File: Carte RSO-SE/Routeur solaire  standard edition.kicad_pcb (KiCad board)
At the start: 2 copper layers, 127.6 x 203.2 mm, 57 parts

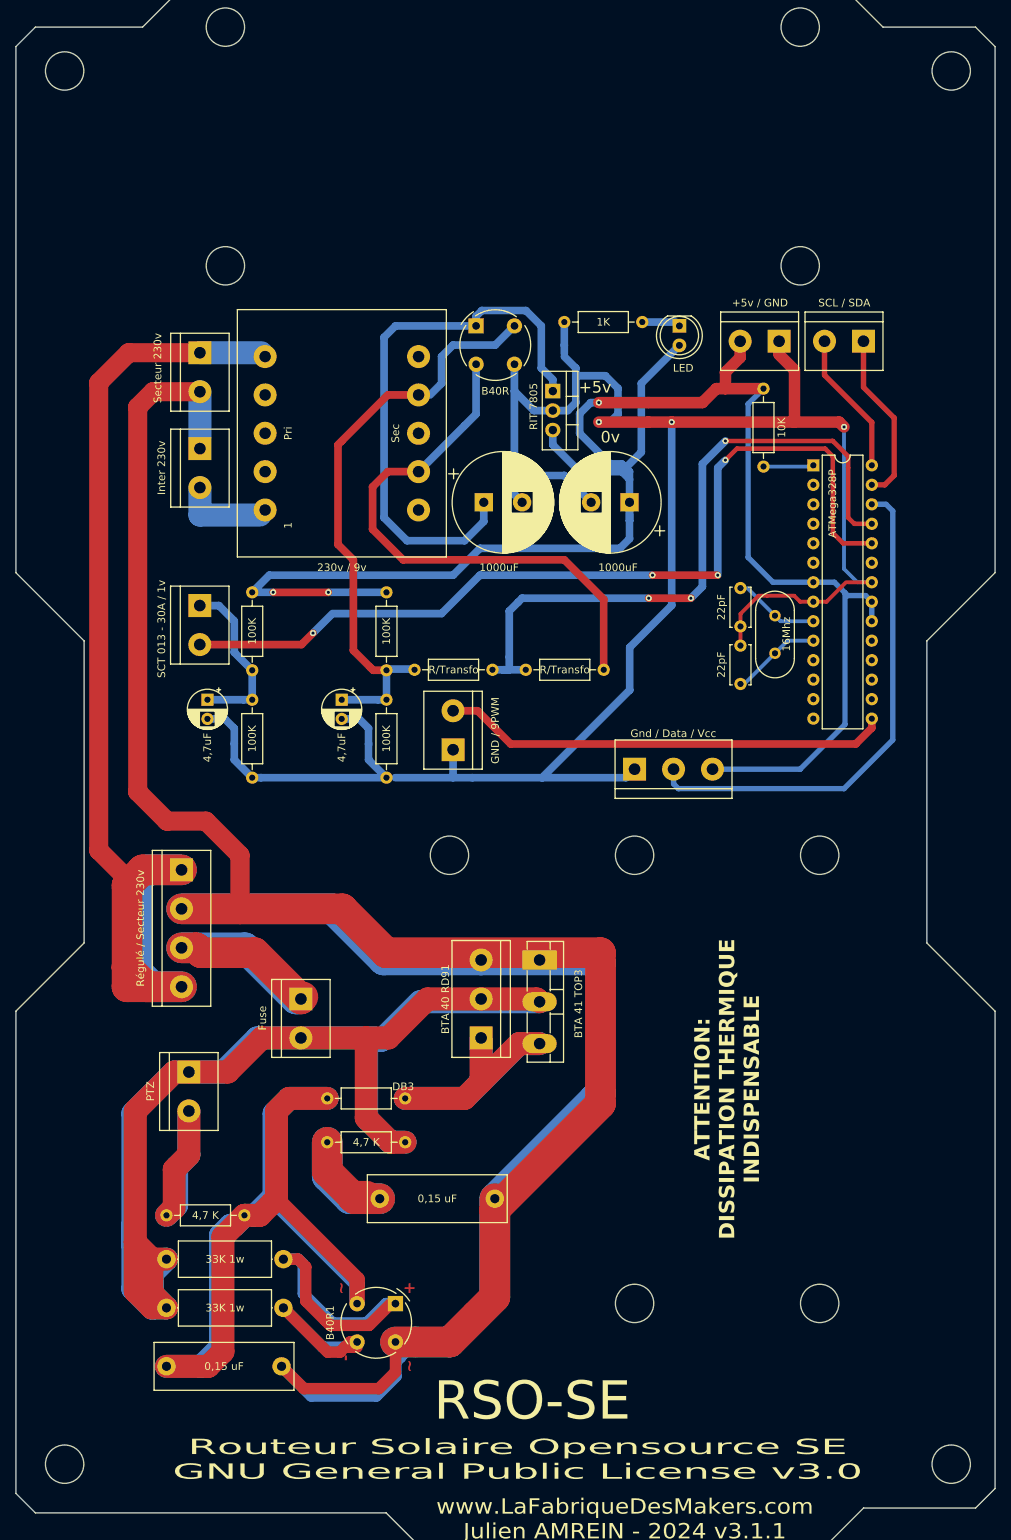
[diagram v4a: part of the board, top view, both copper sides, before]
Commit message: Bornier détection heures creuses
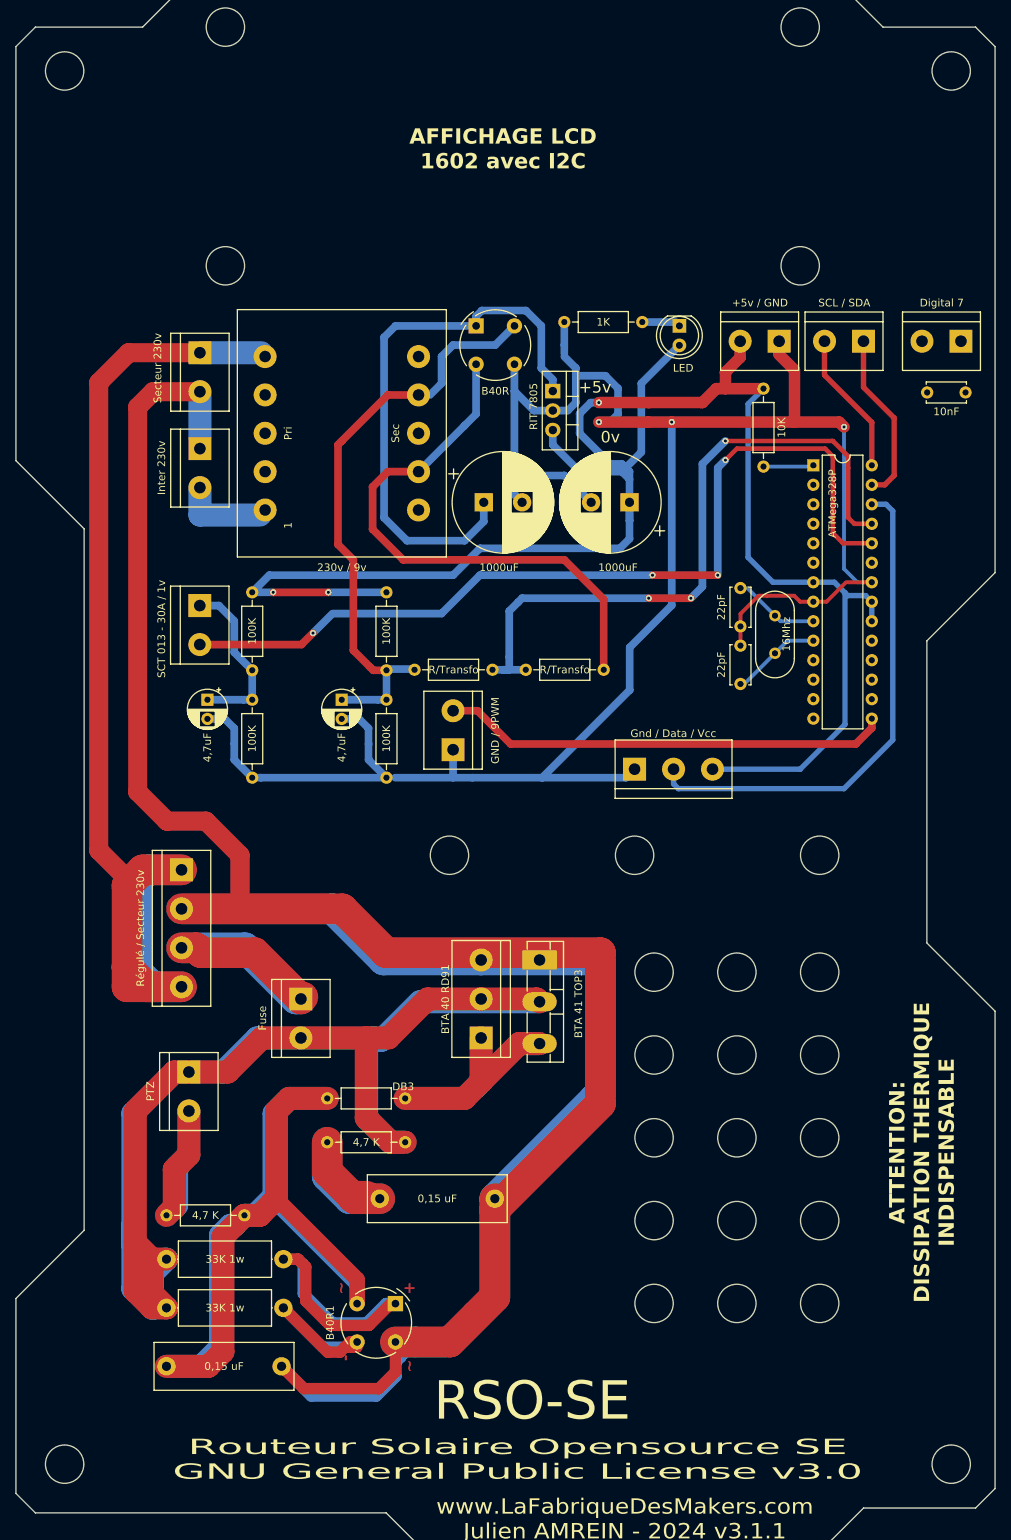
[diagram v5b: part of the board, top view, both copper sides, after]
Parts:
- removed the ? at (-53.3, 167.6)
- added 10nF: C_Disc_D5.0mm_W2.5mm_P5.00mm, Capacitor_THT:C_Disc_D5.0mm_W2.5mm_P5.00mm, F.Cu at (-15.2, 48.9)
- added ?: MountingHole_5mm, MountingHole:MountingHole_5mm, F.Cu at (-50.8, 156.8)
- added ?: MountingHole_5mm, MountingHole:MountingHole_5mm, F.Cu at (-40.0, 124.5)
- added ?: MountingHole_5mm, MountingHole:MountingHole_5mm, F.Cu at (-29.2, 135.3)
- added ?: MountingHole_5mm, MountingHole:MountingHole_5mm, F.Cu at (-29.2, 124.5)
- added ?: MountingHole_5mm, MountingHole:MountingHole_5mm, F.Cu at (-29.2, 156.8)
- added ?: MountingHole_5mm, MountingHole:MountingHole_5mm, F.Cu at (-50.8, 124.5)
- added ?: MountingHole_5mm, MountingHole:MountingHole_5mm, F.Cu at (-40.0, 156.8)
- added ?: MountingHole_5mm, MountingHole:MountingHole_5mm, F.Cu at (-50.8, 135.3)
- added ?: MountingHole_5mm, MountingHole:MountingHole_5mm, F.Cu at (-40.0, 135.3)
- added ?: MountingHole_5mm, MountingHole:MountingHole_5mm, F.Cu at (-50.8, 146.1)
- added ?: MountingHole_5mm, MountingHole:MountingHole_5mm, F.Cu at (-40.0, 146.1)
- added ?: MountingHole_5mm, MountingHole:MountingHole_5mm, F.Cu at (-50.8, 167.6)
- added ?: MountingHole_5mm, MountingHole:MountingHole_5mm, F.Cu at (-40.0, 167.6)
- added ?: MountingHole_5mm, MountingHole:MountingHole_5mm, F.Cu at (-29.2, 146.1)
- added Digital 7: TerminalBlock_bornier-2_P5.08mm, TerminalBlock:TerminalBlock_bornier-2_P5.08mm, F.Cu at (-10.8, 42.2)
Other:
- outline, holes or cut-outs redrawn
- board text added: "AFFICHAGE LCD 1602 avec I2C"

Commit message: RSO Dark edition béta test
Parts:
- removed the 4,7 K at (-93.4, 146.6)
- removed the ? at (-50.8, 156.8)
- removed the ? at (-128.3, -83.8)
- removed the ? at (-29.2, 167.6)
- removed the ? at (-29.2, 124.5)
- removed the ? at (-29.2, 156.8)
- removed the ? at (-50.8, 124.5)
- removed the ? at (-53.3, -114.9)
- removed the ? at (-40.0, 156.8)
- removed the ? at (-53.3, -83.8)
- removed the ? at (-128.3, -114.9)
- removed the ? at (-50.8, 146.1)
- removed the ? at (-50.8, 167.6)
- removed the ? at (-40.0, 167.6)
- removed the ? at (-29.2, 146.1)
- added 10K: R_Axial_DIN0207_L6.3mm_D2.5mm_P10.16mm_Horizontal, Resistor_THT:R_Axial_DIN0207_L6.3mm_D2.5mm_P10.16mm_Horizontal, F.Cu at (-19.1, 48.3)
- added 4,7K: R_Axial_DIN0207_L6.3mm_D2.5mm_P10.16mm_Horizontal, Resistor_THT:R_Axial_DIN0207_L6.3mm_D2.5mm_P10.16mm_Horizontal, F.Cu at (-42.5, 90.8)
- added 4,7K 1w: R_Axial_DIN0414_L11.9mm_D4.5mm_P15.24mm_Horizontal, Resistor_THT:R_Axial_DIN0414_L11.9mm_D4.5mm_P15.24mm_Horizontal, F.Cu at (-93.3, 146.7)
- added ?: MountingHole_5mm, MountingHole:MountingHole_5mm, F.Cu at (-58.4, 5.71)
- added ?: MountingHole_5mm, MountingHole:MountingHole_5mm, F.Cu at (-90.8, 5.71)
- added ?: MountingHole_5mm, MountingHole:MountingHole_5mm, F.Cu at (-69.2, 24.8)
- added ?: MountingHole_5mm, MountingHole:MountingHole_5mm, F.Cu at (-69.2, 5.71)
- added ?: MountingHole_5mm, MountingHole:MountingHole_5mm, F.Cu at (-58.4, 24.8)
- added ?: MountingHole_5mm, MountingHole:MountingHole_5mm, F.Cu at (-47.6, 5.71)
- added ?: MountingHole_5mm, MountingHole:MountingHole_5mm, F.Cu at (-47.6, 24.8)
- added ?: MountingHole_5mm, MountingHole:MountingHole_5mm, F.Cu at (-80.0, 24.8)
- added ?: MountingHole_5mm, MountingHole:MountingHole_5mm, F.Cu at (-80.0, 5.71)
- added ?: MountingHole_5mm, MountingHole:MountingHole_5mm, F.Cu at (-90.8, 24.8)
- added Jour nuit: TerminalBlock_bornier-2_P5.08mm, TerminalBlock:TerminalBlock_bornier-2_P5.08mm, F.Cu at (-10.8, 31.1)
- 33K 3w: renamed from 33K 1w (x2)
- Inter hiver: renamed from Digital 7
- moved ? 30.5 mm to (-28.6, 165.7)
- moved ? 30.5 mm to (-50.2, 165.7)
- moved ? 30.5 mm to (-39.4, 165.7)
- moved ? 30.5 mm to (-39.4, 154.9)
- moved ? 30.5 mm to (-39.4, 176.5)
- moved ? 18.0 mm to (-95.2, 106.7)
- moved 10nF 17.9 mm to (-17.1, 31.1), turned to 90 degrees
- moved ? 12.1 mm to (-65.4, 108.6)
- moved ? 11.9 mm to (-24.1, 120.0)
- turned Inter hiver to 90 degrees
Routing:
- net (no net): track 2323.2 -> 2514.8 mm, vias 13 -> 14
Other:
- outline, holes or cut-outs redrawn
- board text added: "D7"
- board text added: "DS18B20"
- board text added: "RSO-DE"
- board text removed: "RSO-SE"

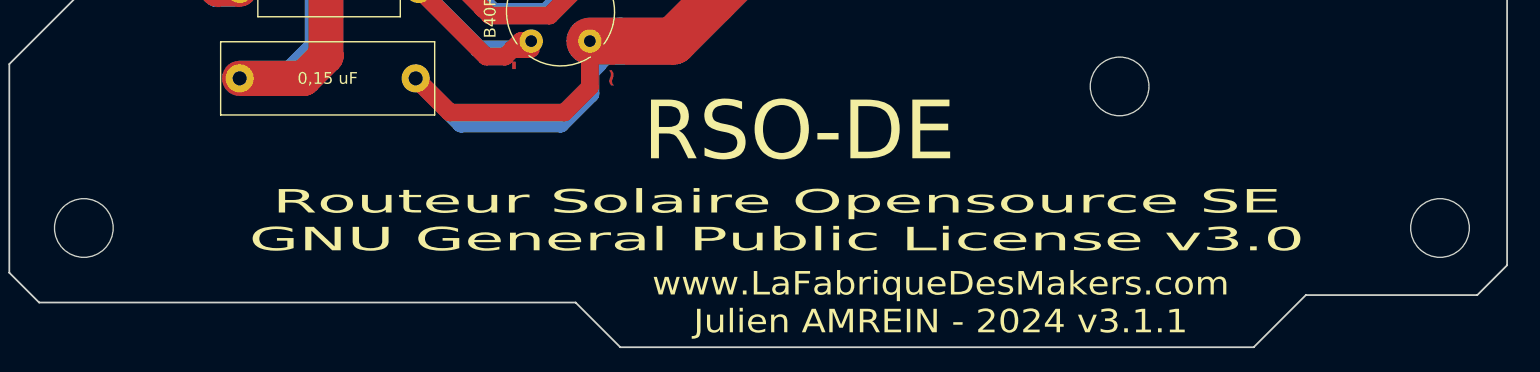
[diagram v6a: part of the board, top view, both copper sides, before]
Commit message: MAJ Importante sortie de boucle
Sortie de boucle pour le cas 3 de gestion de température
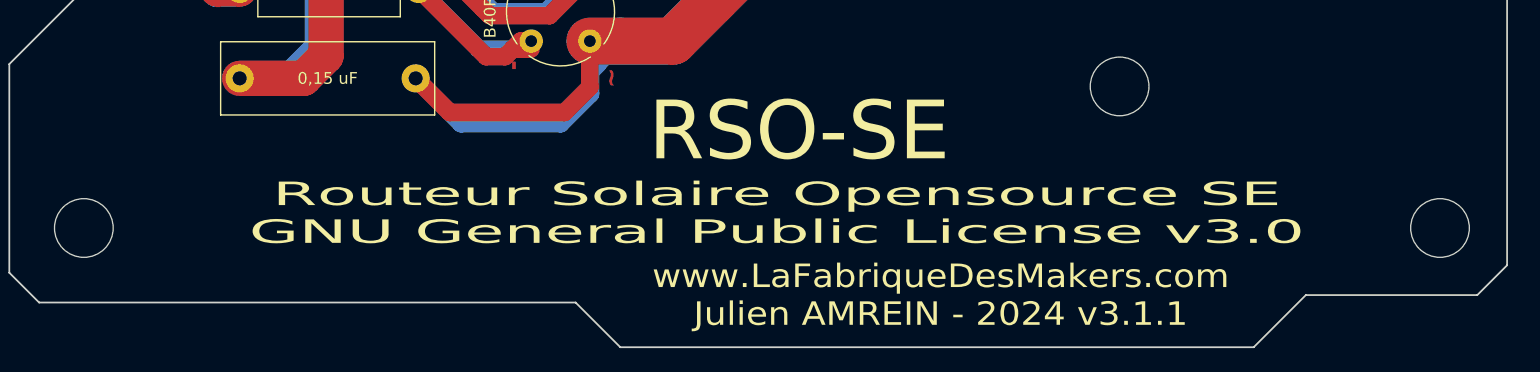
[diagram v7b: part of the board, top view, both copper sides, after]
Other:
- board text added: "RSO-SE"
- board text removed: "RSO-DE"
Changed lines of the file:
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@@
     (effects (font (size 1.5 1.5) (thickness 0.3) bold) (justify left bottom))
   )
-  (gr_text "Routeur Solaire Opensource SE\nGNU General Public License v3.0" (at -68.58 187.96) (layer "F.SilkS")
+  (gr_text "Routeur Solaire Opensource SE\nGNU General Public License v3.0" (at -68.58 187.325) (layer "F.SilkS")
     (effects (font (size 2 4) (thickness 0.25)))
   )
@@
     (effects (font (size 1.5 1.5) (thickness 0.3)))
   )
-  (gr_text "RSO-DE" (at -66.675 180.34) (layer "F.SilkS")
+  (gr_text "RSO-SE" (at -66.675 180.34) (layer "F.SilkS")
     (effects (font (size 5 5) (thickness 1)))
   )
@@
     (effects (font (size 2 2) (thickness 0.4) bold))
   )
-  (gr_text "www.LaFabriqueDesMakers.com\nJulien AMREIN - 2024 v3.1.1" (at -54.61 194.945) (layer "F.SilkS")
+  (gr_text "www.LaFabriqueDesMakers.com\nJulien AMREIN - 2024 v3.1.1" (at -54.61 194.31) (layer "F.SilkS")
     (effects (font (size 2 2.2) (thickness 0.25)))
   )
